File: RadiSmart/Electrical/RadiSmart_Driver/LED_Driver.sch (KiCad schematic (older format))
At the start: 68 parts, among them U1 BTF6070-2EKV, U2 BTF6070-2EKV, U3 LM3406_LED_Driver, U4 LM3406_LED_Driver, U5 LM3406_LED_Driver, U6 LM3406_LED_Driver

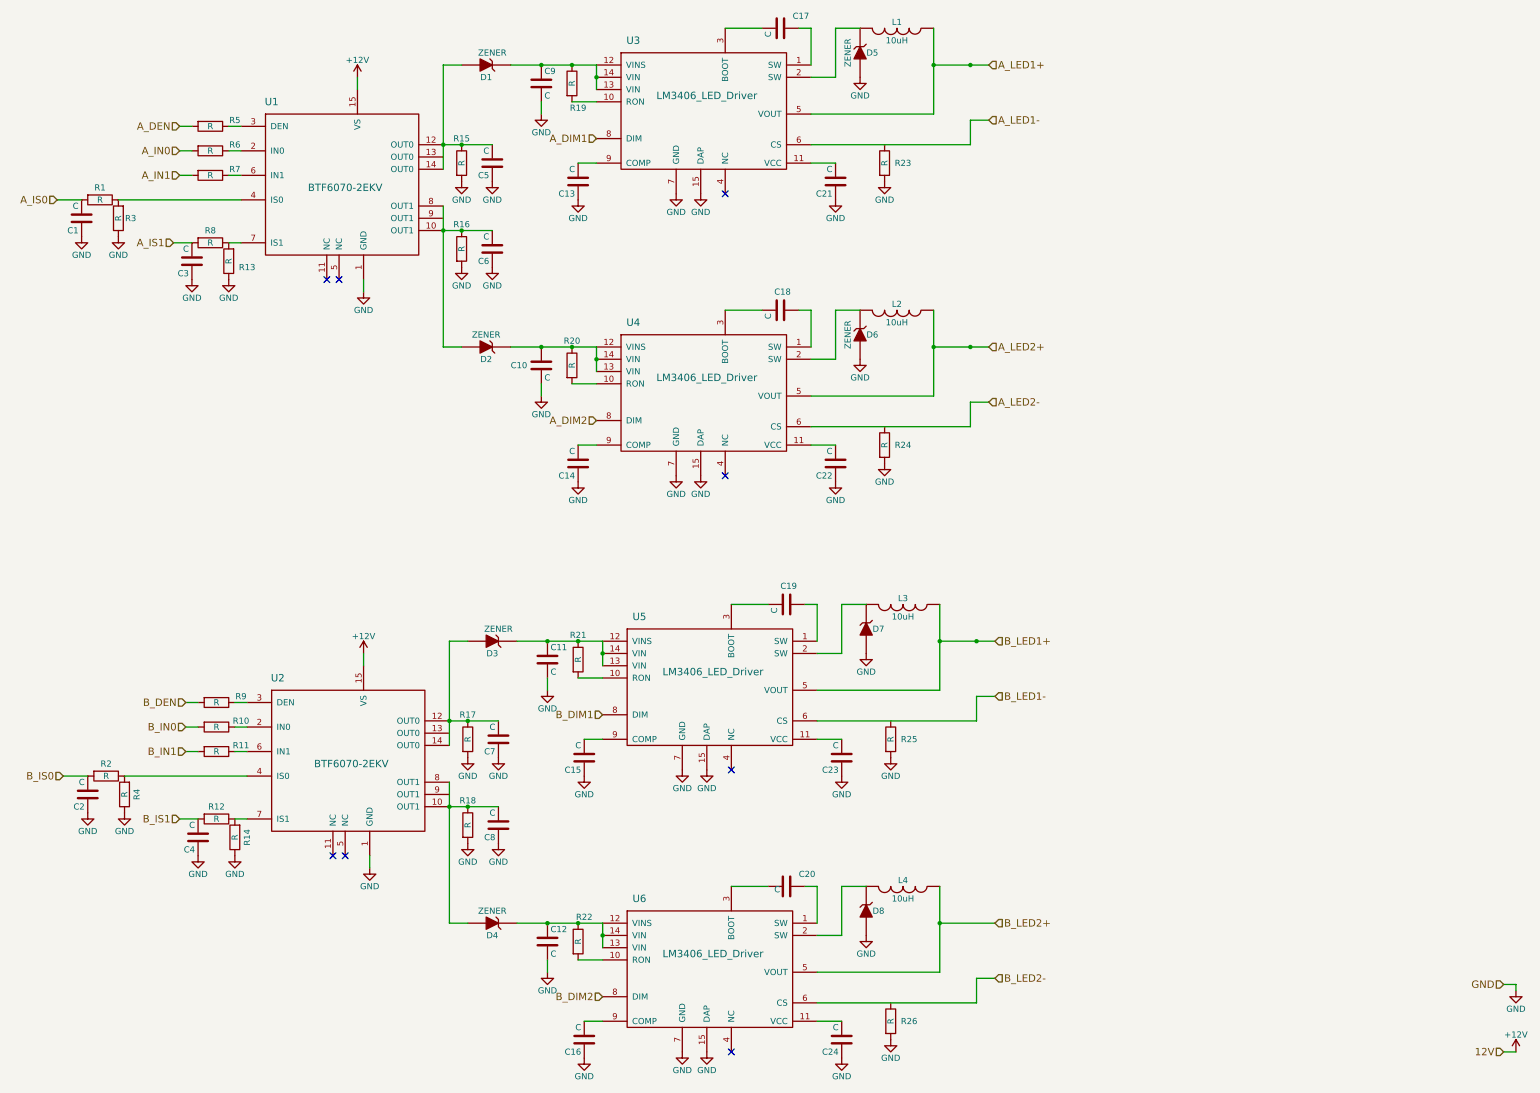
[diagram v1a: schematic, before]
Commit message: switching from 12V to 24V to support more LEDs per channel
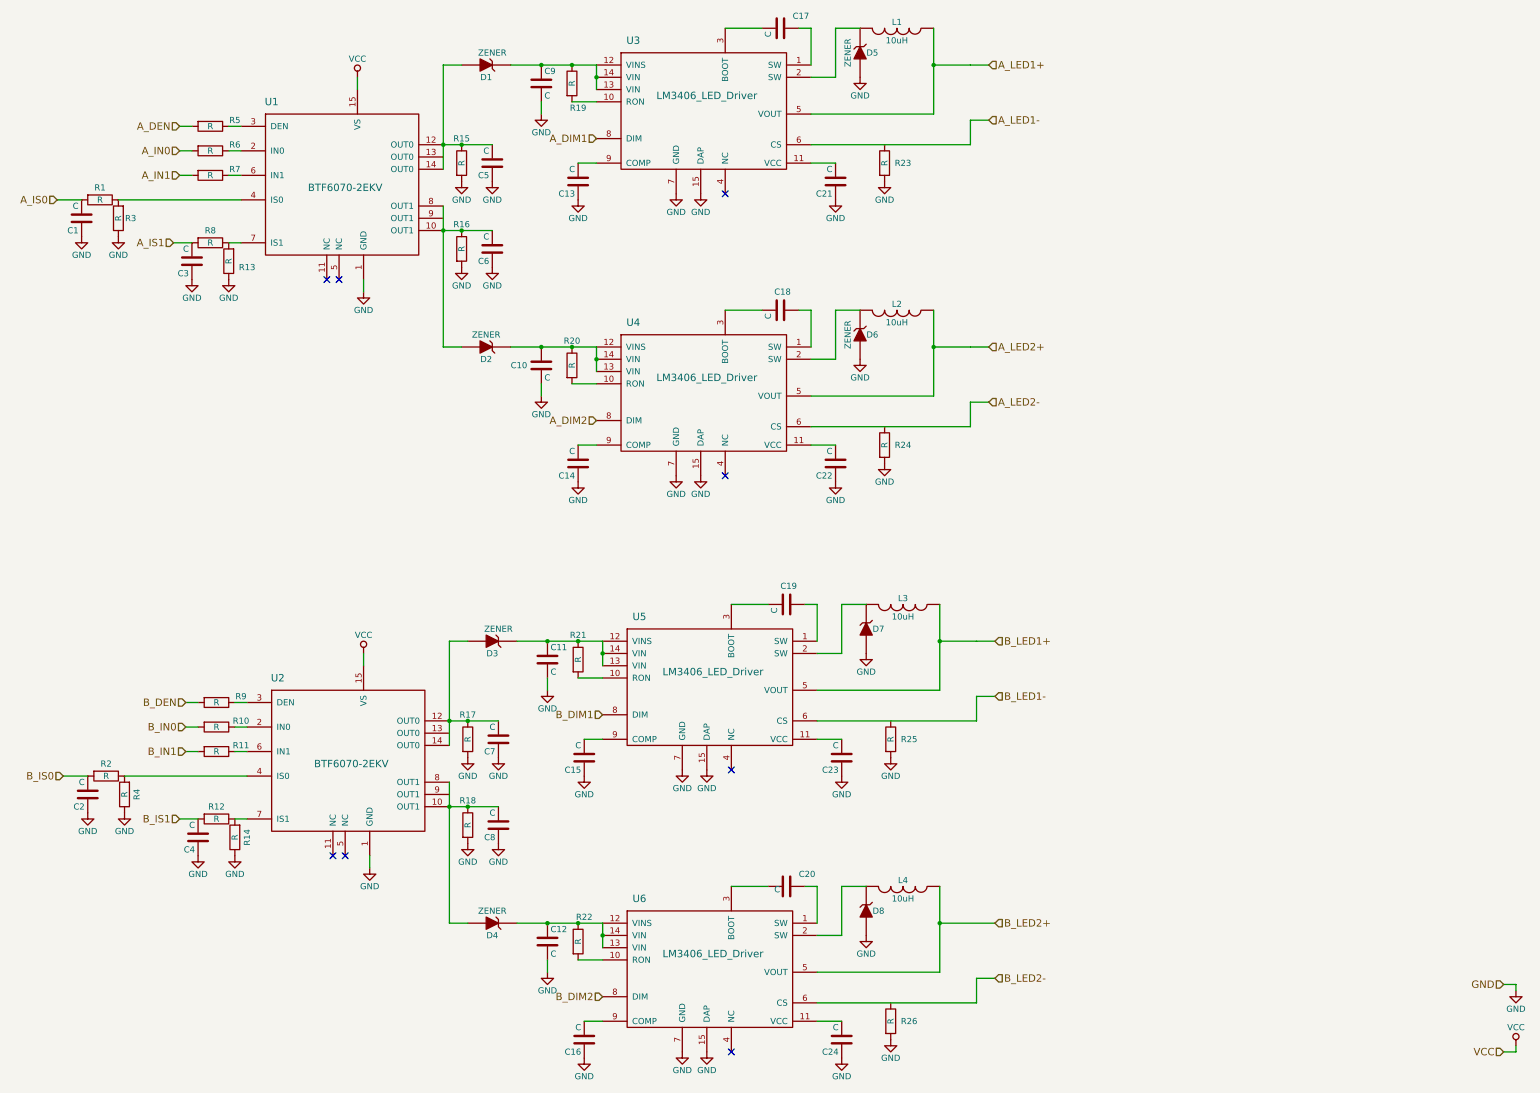
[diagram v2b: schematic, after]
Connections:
- net +12V renamed VCC
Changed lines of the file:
@@
 LIBS:contrib
 LIBS:valves
+LIBS:MRV_ICs
 LIBS:RadiSmart_Driver-cache
 EELAYER 25 0
@@
 $EndComp
 Text HLabel 15600 9800 0    60   Input ~ 0
-12V
+VCC
 Text HLabel 8200 2350 0    60   Input ~ 0
 A_DIM1
@@
 A_LED2-
 $Comp
-L +12V #PWR027
-U 1 1 59F3F466
-P 6250 1850
-F 0 "#PWR027" H 6250 1700 50  0001 C CNN
-F 1 "+12V" H 6250 1990 50  0000 C CNN
-F 2 "" H 6250 1850 50  0000 C CNN
-F 3 "" H 6250 1850 50  0000 C CNN
-	1    6250 1850
-	1    0    0    -1
-$EndComp
-$Comp
 L BTF6070-2EKV U1
 U 1 1 59F4574B
@@
 $EndComp
 $Comp
-L +12V #PWR028
-U 1 1 59F45F6B
-P 15700 9800
-F 0 "#PWR028" H 15700 9650 50  0001 C CNN
-F 1 "+12V" H 15700 9940 50  0000 C CNN
-F 2 "" H 15700 9800 50  0000 C CNN
-F 3 "" H 15700 9800 50  0000 C CNN
-	1    15700 9800
-	1    0    0    -1
-$EndComp
-$Comp
 L GND #PWR029
 U 1 1 59F478E5
@@
 $EndComp
 Wire Wire Line
-	7500 1750 8200 1750
+	7500 1750 7750 1750
+Wire Wire Line
+	7750 1750 8000 1750
+Wire Wire Line
+	8000 1750 8200 1750
 Connection ~ 7750 1750
 Connection ~ 8000 1750
@@
 	9950 1450 9950 1750
 Wire Wire Line
-	8200 1750 8200 1950
+	8200 1750 8200 1850
+Wire Wire Line
+	8200 1850 8200 1950
 Connection ~ 8200 1850
 Wire Wire Line
@@
 	10950 2150 9950 2150
 Wire Wire Line
-	10950 1450 10950 2150
-Wire Wire Line
-	10950 1750 11400 1750
+	10950 1450 10950 1750
+Wire Wire Line
+	10950 1750 10950 2150
+Wire Wire Line
+	10950 1750 11250 1750
+Wire Wire Line
+	11250 1750 11400 1750
 Connection ~ 10950 1750
 Wire Wire Line
@@
 Wire Wire Line
 	11400 2200 11250 2200
-Connection ~ 11250 1750
-Wire Wire Line
-	7500 4050 8200 4050
+Wire Wire Line
+	7500 4050 7750 4050
+Wire Wire Line
+	7750 4050 8000 4050
+Wire Wire Line
+	8000 4050 8200 4050
 Connection ~ 7750 4050
 Connection ~ 8000 4050
@@
 	9950 3750 9950 4050
 Wire Wire Line
-	8200 4050 8200 4250
+	8200 4050 8200 4150
+Wire Wire Line
+	8200 4150 8200 4250
 Connection ~ 8200 4150
 Wire Wire Line
@@
 	10950 4450 9950 4450
 Wire Wire Line
-	10950 3750 10950 4450
-Wire Wire Line
-	10950 4050 11400 4050
+	10950 3750 10950 4050
+Wire Wire Line
+	10950 4050 10950 4450
+Wire Wire Line
+	11250 4050 11400 4050
 Connection ~ 10950 4050
 Wire Wire Line
@@
 Wire Wire Line
 	11400 4500 11250 4500
-Connection ~ 11250 4050
 Wire Wire Line
 	15600 9800 15700 9800
@@
 	7750 2050 7750 2150
 Wire Wire Line
-	6950 1750 6950 2600
+	6950 1750 6950 2400
+Wire Wire Line
+	6950 2400 6950 2600
 Wire Wire Line
 	6950 1750 7100 1750
 Connection ~ 6950 2400
 Wire Wire Line
-	6950 2900 6950 4050
+	6950 2900 6950 3100
+Wire Wire Line
+	6950 3100 6950 4050
 Wire Wire Line
 	6950 4050 7100 4050
@@
 	5200 2250 5300 2250
 Wire Wire Line
-	6950 2400 7350 2400
+	6950 2400 7100 2400
+Wire Wire Line
+	7100 2400 7350 2400
 Connection ~ 7100 2400
 Wire Wire Line
-	6950 3100 7350 3100
+	6950 3100 7100 3100
+Wire Wire Line
+	7100 3100 7350 3100
 Connection ~ 7100 3100
 $Comp
@@
 B_LED2-
 $Comp
-L +12V #PWR053
-U 1 1 59F53962
-P 6300 6550
-F 0 "#PWR053" H 6300 6400 50  0001 C CNN
-F 1 "+12V" H 6300 6690 50  0000 C CNN
-F 2 "" H 6300 6550 50  0000 C CNN
-F 3 "" H 6300 6550 50  0000 C CNN
-	1    6300 6550
-	1    0    0    -1
-$EndComp
-$Comp
 L BTF6070-2EKV U2
 U 1 1 59F53968
@@
 $EndComp
 Wire Wire Line
-	7550 6450 8250 6450
+	7550 6450 7800 6450
+Wire Wire Line
+	7800 6450 8050 6450
+Wire Wire Line
+	8050 6450 8250 6450
 Connection ~ 7800 6450
 Connection ~ 8050 6450
@@
 	10000 6150 10000 6450
 Wire Wire Line
-	8250 6450 8250 6650
+	8250 6450 8250 6550
+Wire Wire Line
+	8250 6550 8250 6650
 Connection ~ 8250 6550
 Wire Wire Line
@@
 	11000 6850 10000 6850
 Wire Wire Line
-	11000 6150 11000 6850
-Wire Wire Line
-	11000 6450 11450 6450
+	11000 6150 11000 6450
+Wire Wire Line
+	11000 6450 11000 6850
+Wire Wire Line
+	11000 6450 11300 6450
+Wire Wire Line
+	11300 6450 11450 6450
 Connection ~ 11000 6450
 Wire Wire Line
@@
 Wire Wire Line
 	11450 6900 11300 6900
-Connection ~ 11300 6450
-Wire Wire Line
-	7550 8750 8250 8750
+Wire Wire Line
+	7550 8750 7800 8750
+Wire Wire Line
+	7800 8750 8050 8750
+Wire Wire Line
+	8050 8750 8250 8750
 Connection ~ 7800 8750
 Connection ~ 8050 8750
@@
 	10000 8450 10000 8750
 Wire Wire Line
-	8250 8750 8250 8950
+	8250 8750 8250 8850
+Wire Wire Line
+	8250 8850 8250 8950
 Connection ~ 8250 8850
 Wire Wire Line
@@
 	11000 9150 10000 9150
 Wire Wire Line
-	11000 8450 11000 9150
+	11000 8450 11000 8750
+Wire Wire Line
+	11000 8750 11000 9150
 Wire Wire Line
 	11000 8750 11450 8750
@@
 	7800 6750 7800 6850
 Wire Wire Line
-	7000 6450 7000 7300
+	7000 6450 7000 7100
+Wire Wire Line
+	7000 7100 7000 7300
 Wire Wire Line
 	7000 6450 7150 6450
 Connection ~ 7000 7100
 Wire Wire Line
-	7000 7600 7000 8750
+	7000 7600 7000 7800
+Wire Wire Line
+	7000 7800 7000 8750
 Wire Wire Line
 	7000 8750 7150 8750
@@
 	5250 6950 5350 6950
 Wire Wire Line
-	7000 7100 7400 7100
+	7000 7100 7150 7100
+Wire Wire Line
+	7150 7100 7400 7100
 Connection ~ 7150 7100
 Wire Wire Line
-	7000 7800 7400 7800
+	7000 7800 7150 7800
+Wire Wire Line
+	7150 7800 7400 7800
 Connection ~ 7150 7800
 $Comp
@@
 	0    1    1    0
 $EndComp
+$Comp
+L VCC #PWR?
+U 1 1 5A06008A
+P 15700 9750
+F 0 "#PWR?" H 15700 9600 50  0001 C CNN
+F 1 "VCC" H 15700 9900 50  0000 C CNN
+F 2 "" H 15700 9750 50  0000 C CNN
+F 3 "" H 15700 9750 50  0000 C CNN
+	1    15700 9750
+	1    0    0    -1
+$EndComp
+Wire Wire Line
+	15700 9800 15700 9750
+$Comp
+L VCC #PWR?
+U 1 1 5A06049C
+P 6300 6550
+F 0 "#PWR?" H 6300 6400 50  0001 C CNN
+F 1 "VCC" H 6300 6700 50  0000 C CNN
+F 2 "" H 6300 6550 50  0000 C CNN
+F 3 "" H 6300 6550 50  0000 C CNN
+	1    6300 6550
+	1    0    0    -1
+$EndComp
+$Comp
+L VCC #PWR?
+U 1 1 5A060B23
+P 6250 1850
+F 0 "#PWR?" H 6250 1700 50  0001 C CNN
+F 1 "VCC" H 6250 2000 50  0000 C CNN
+F 2 "" H 6250 1850 50  0000 C CNN
+F 3 "" H 6250 1850 50  0000 C CNN
+	1    6250 1850
+	1    0    0    -1
+$EndComp
+Wire Wire Line
+	10950 4050 11250 4050
 $EndSCHEMATC
